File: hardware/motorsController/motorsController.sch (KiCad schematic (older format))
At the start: 1 part

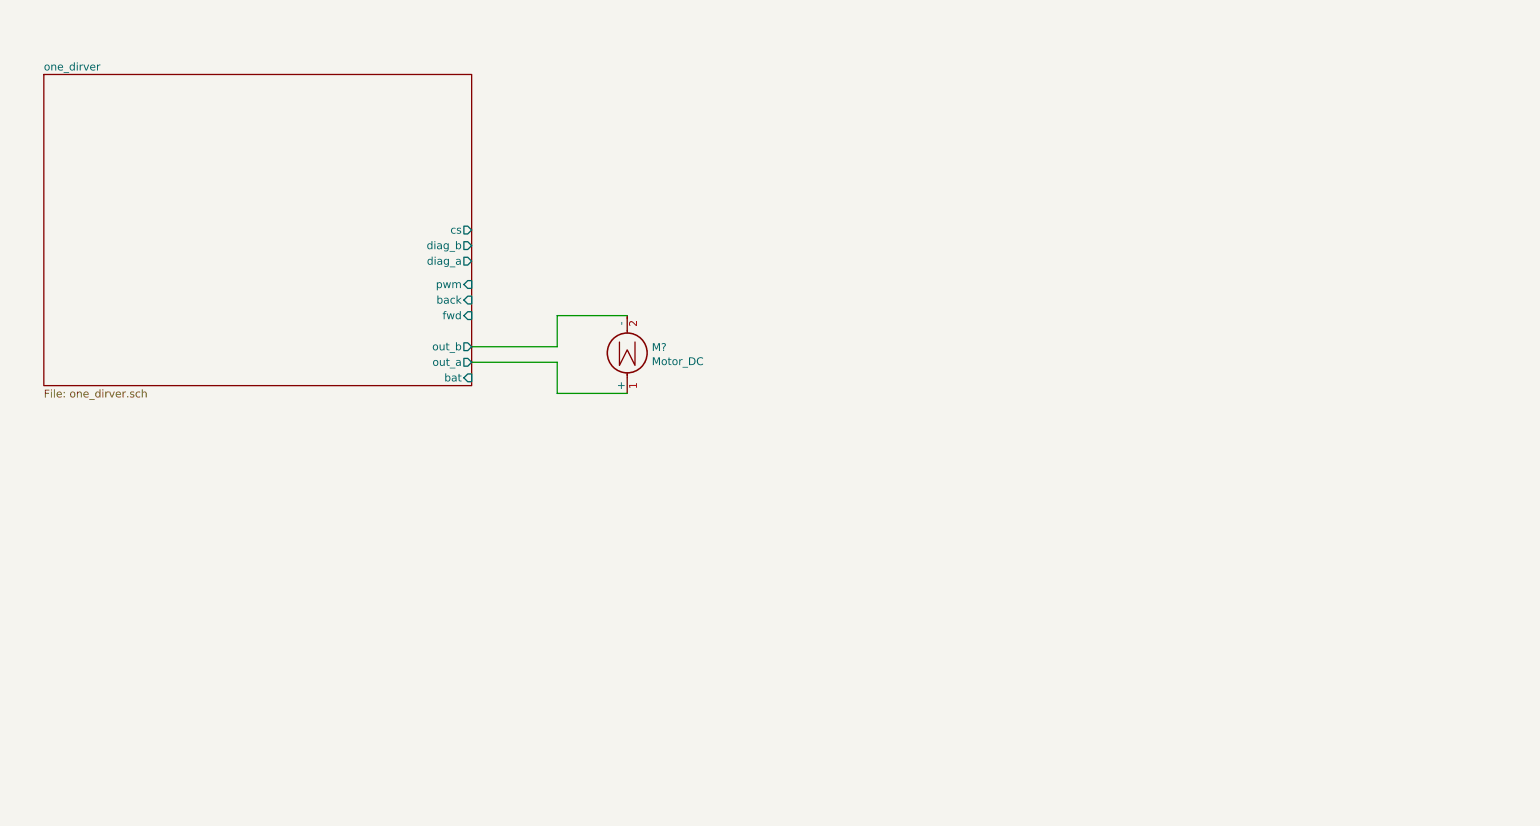
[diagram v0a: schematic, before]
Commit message: layout a pcb for the motor driver IC
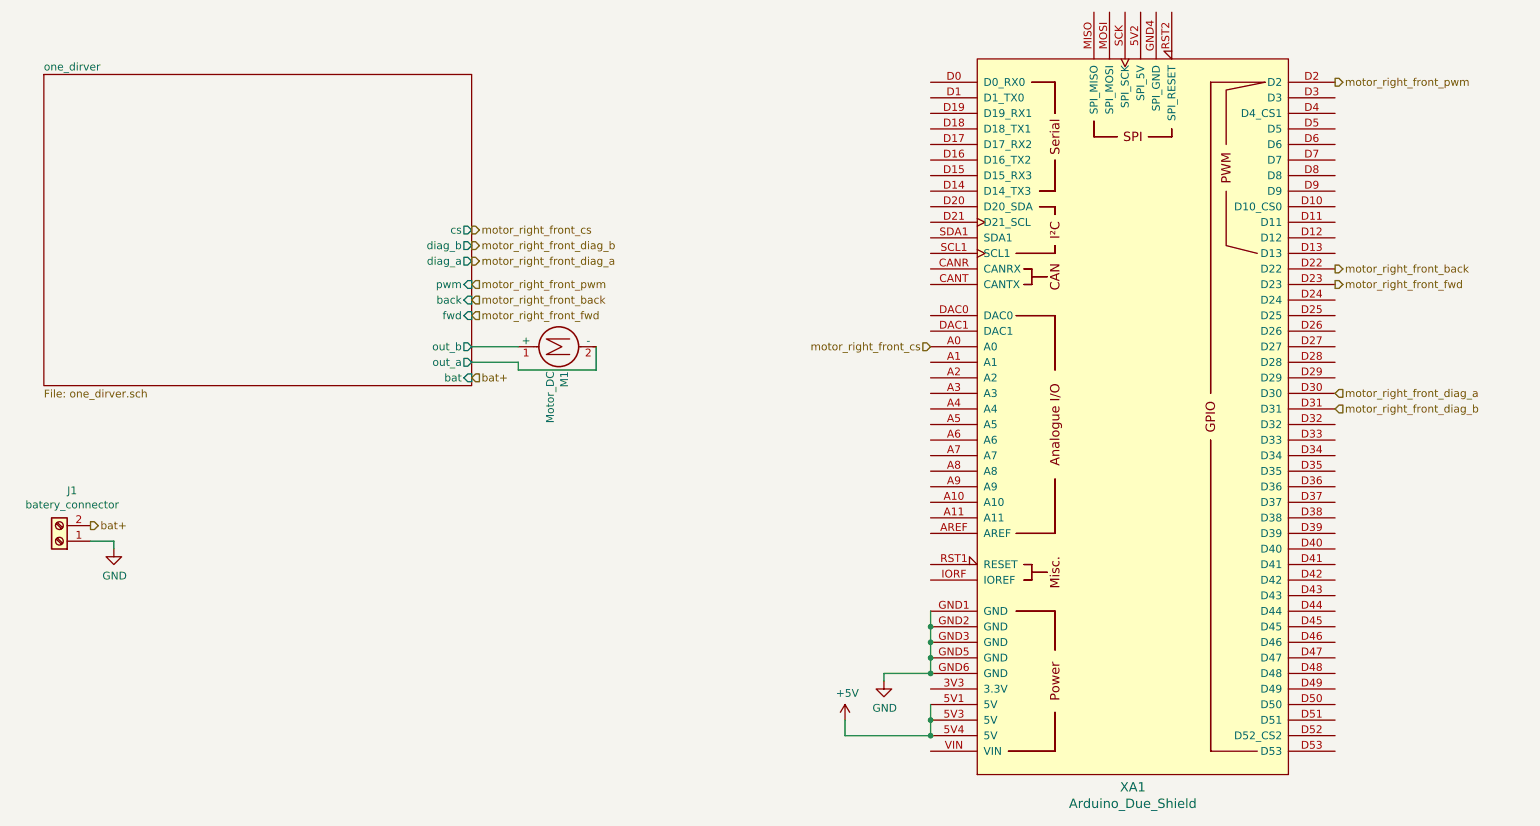
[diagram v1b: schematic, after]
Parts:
- added J1: batery_connector, TerminalBlock:TerminalBlock_bornier-2_P5.08mm, symbol Connector:Screw_Terminal_01x02
- added XA1: Arduino_Due_Shield, Arduino:Arduino_Due_Shield, symbol arduino:Arduino_Due_Shield
- M1: renamed from M?; footprint (none) -> TerminalBlock:TerminalBlock_bornier-2_P5.08mm
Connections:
- net one_dirver/out_a: now also M1.2 (-); no longer M1.1 (+)
- net one_dirver/out_b: now also M1.1 (+); no longer M1.2 (-)
- new net +5V: XA1.5V1 (5V), XA1.5V3 (5V), XA1.5V4 (5V)
- new net GND: J1.1 (Pin_1), XA1.GND1 (GND), XA1.GND2 (GND), XA1.GND3 (GND), XA1.GND5 (GND), XA1.GND6 (GND)
- new net bat+: J1.2 (Pin_2)
- new net motor_right_front_back: XA1.D22
- new net motor_right_front_cs: XA1.A0
- new net motor_right_front_diag_a: XA1.D30
- new net motor_right_front_diag_b: XA1.D31
- new net motor_right_front_fwd: XA1.D23
- new net motor_right_front_pwm: XA1.D2
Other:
- moved on the sheet: M1
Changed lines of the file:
@@
 EELAYER 30 0
 EELAYER END
-$Descr A4 11693 8268
+$Descr A3 16535 11693
 encoding utf-8
 Sheet 1 2
@@
 F10 "bat" I R 4000 3150 50
 $EndSheet
+Text HLabel 4000 2550 2    50   Input ~ 0
+motor_right_front_pwm
 $Comp
-L Motor:Motor_DC M?
+L Motor:Motor_DC M1
 U 1 1 5F794D70
-P 5000 3050
-F 0 "M?" H 4842 2954 50  0000 R CNN
-F 1 "Motor_DC" H 4842 3045 50  0000 R CNN
-F 2 "" H 5000 2960 50  0001 C CNN
-F 3 "~" H 5000 2960 50  0001 C CNN
-	1    5000 3050
+P 4500 2950
+F 0 "M1" H 4342 2854 50  0000 R CNN
+F 1 "Motor_DC" H 4342 2945 50  0000 R CNN
+F 2 "TerminalBlock:TerminalBlock_bornier-2_P5.08mm" H 4500 2860 50  0001 C CNN
+F 3 "~" H 4500 2860 50  0001 C CNN
+	1    4500 2950
+	0    -1   -1   0
+$EndComp
+Wire Wire Line
+	4300 2950 4000 2950
+Wire Wire Line
+	4800 2950 4800 3100
+Wire Wire Line
+	4800 3100 4300 3100
+Wire Wire Line
+	4300 3100 4300 3050
+Wire Wire Line
+	4300 3050 4000 3050
+Text HLabel 4000 2650 2    50   Input ~ 0
+motor_right_front_back
+Text HLabel 4000 2750 2    50   Input ~ 0
+motor_right_front_fwd
+Text HLabel 4000 2200 2    50   Output ~ 0
+motor_right_front_cs
+Text HLabel 4000 2300 2    50   Output ~ 0
+motor_right_front_diag_b
+Text HLabel 4000 2400 2    50   Output ~ 0
+motor_right_front_diag_a
+Text HLabel 9550 1250 2    50   Output ~ 0
+motor_right_front_pwm
+Text HLabel 9550 2450 2    50   Output ~ 0
+motor_right_front_back
+Text HLabel 9550 2550 2    50   Output ~ 0
+motor_right_front_fwd
+Text HLabel 6950 2950 0    50   Input ~ 0
+motor_right_front_cs
+Text HLabel 9550 3350 2    50   Input ~ 0
+motor_right_front_diag_b
+Text HLabel 9550 3250 2    50   Input ~ 0
+motor_right_front_diag_a
+$Comp
+L power:GND #PWR0105
+U 1 1 5F7FA8F7
+P 6650 5100
+F 0 "#PWR0105" H 6650 4850 50  0001 C CNN
+F 1 "GND" H 6655 4927 50  0000 C CNN
+F 2 "" H 6650 5100 50  0001 C CNN
+F 3 "" H 6650 5100 50  0001 C CNN
+	1    6650 5100
+	1    0    0    -1
+$EndComp
+Wire Wire Line
+	6650 5100 6650 5050
+Wire Wire Line
+	6650 5050 6950 5050
+$Comp
+L power:+5V #PWR0106
+U 1 1 5F7FCF51
+P 6400 5350
+F 0 "#PWR0106" H 6400 5200 50  0001 C CNN
+F 1 "+5V" H 6415 5523 50  0000 C CNN
+F 2 "" H 6400 5350 50  0001 C CNN
+F 3 "" H 6400 5350 50  0001 C CNN
+	1    6400 5350
+	1    0    0    -1
+$EndComp
+Wire Wire Line
+	6400 5350 6400 5450
+Wire Wire Line
+	6400 5450 6950 5450
+$Comp
+L Connector:Screw_Terminal_01x02 J1
+U 1 1 5F7F2610
+P 1350 4200
+F 0 "J1" H 1268 3875 50  0000 C CNN
+F 1 "batery_connector" H 1268 3966 50  0000 C CNN
+F 2 "TerminalBlock:TerminalBlock_bornier-2_P5.08mm" H 1350 4200 50  0001 C CNN
+F 3 "~" H 1350 4200 50  0001 C CNN
+	1    1350 4200
 	-1   0    0    1
 $EndComp
+$Comp
+L power:GND #PWR0107
+U 1 1 5F7F3543
+P 1700 4250
+F 0 "#PWR0107" H 1700 4000 50  0001 C CNN
+F 1 "GND" H 1705 4077 50  0000 C CNN
+F 2 "" H 1700 4250 50  0001 C CNN
+F 3 "" H 1700 4250 50  0001 C CNN
+	1    1700 4250
+	1    0    0    -1
+$EndComp
 Wire Wire Line
-	5000 2750 4550 2750
+	1700 4250 1700 4200
 Wire Wire Line
-	4550 2750 4550 2950
+	1700 4200 1550 4200
+Text HLabel 1550 4100 2    50   Output ~ 0
+bat+
+Text HLabel 4000 3150 2    50   Input ~ 0
+bat+
+$Comp
+L arduino:Arduino_Due_Shield XA1
+U 1 1 5F7F0EA5
+P 8250 3400
+F 0 "XA1" H 8250 1019 60  0000 C CNN
+F 1 "Arduino_Due_Shield" H 8250 913 60  0000 C CNN
+F 2 "Arduino:Arduino_Due_Shield" H 8950 6150 60  0001 C CNN
+F 3 "https://store.arduino.cc/arduino-due" H 8950 6150 60  0001 C CNN
+	1    8250 3400
+	1    0    0    -1
+$EndComp
 Wire Wire Line
-	4550 2950 4000 2950
+	6950 5450 6950 5350
+Connection ~ 6950 5450
+Connection ~ 6950 5350
 Wire Wire Line
-	5000 3250 4550 3250
+	6950 5350 6950 5250
 Wire Wire Line
-	4550 3250 4550 3050
+	6950 5050 6950 4950
+Connection ~ 6950 5050
+Connection ~ 6950 4750
 Wire Wire Line
-	4550 3050 4000 3050
+	6950 4750 6950 4650
+Connection ~ 6950 4850
+Wire Wire Line
+	6950 4850 6950 4750
+Connection ~ 6950 4950
+Wire Wire Line
+	6950 4950 6950 4850
 $EndSCHEMATC

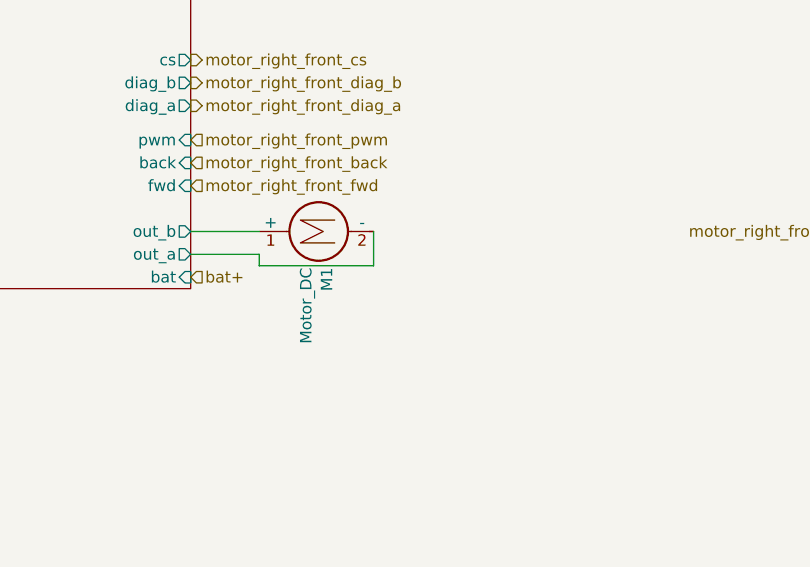
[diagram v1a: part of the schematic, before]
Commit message: reposition motor terminals on both sides of the dirver
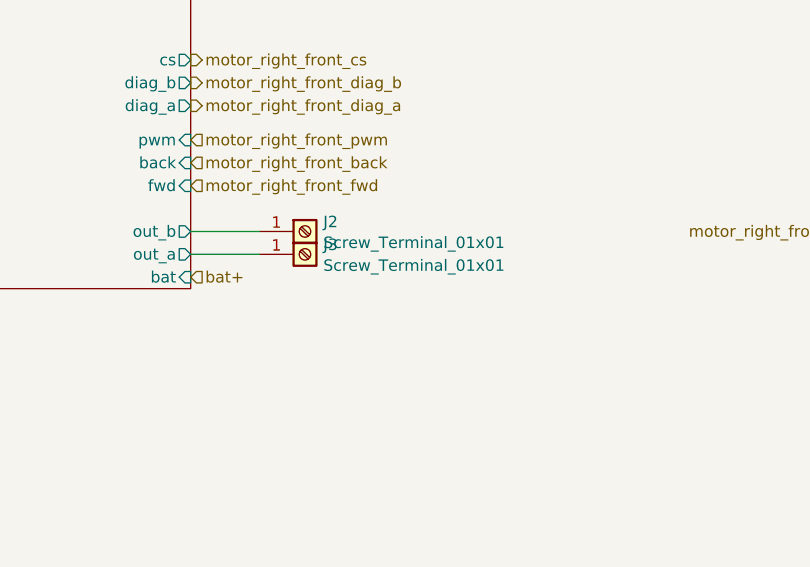
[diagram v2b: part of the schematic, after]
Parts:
- removed M1: Motor_DC, TerminalBlock:TerminalBlock_bornier-2_P5.08mm, symbol Motor:Motor_DC
- added J2, J3: Screw_Terminal_01x01, Connector_Pin:Pin_D1.3mm_L11.3mm_W2.8mm_Flat, symbol Connector:Screw_Terminal_01x01
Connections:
- net one_dirver/out_a: now also J3.1 (Pin_1)
- net one_dirver/out_b: now also J2.1 (Pin_1)
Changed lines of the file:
@@
 Text HLabel 4000 2550 2    50   Input ~ 0
 motor_right_front_pwm
-$Comp
-L Motor:Motor_DC M1
-U 1 1 5F794D70
-P 4500 2950
-F 0 "M1" H 4342 2854 50  0000 R CNN
-F 1 "Motor_DC" H 4342 2945 50  0000 R CNN
-F 2 "TerminalBlock:TerminalBlock_bornier-2_P5.08mm" H 4500 2860 50  0001 C CNN
-F 3 "~" H 4500 2860 50  0001 C CNN
-	1    4500 2950
-	0    -1   -1   0
-$EndComp
 Wire Wire Line
 	4300 2950 4000 2950
-Wire Wire Line
-	4800 2950 4800 3100
-Wire Wire Line
-	4800 3100 4300 3100
-Wire Wire Line
-	4300 3100 4300 3050
 Wire Wire Line
 	4300 3050 4000 3050
@@
 Wire Wire Line
 	6950 4950 6950 4850
+$Comp
+L Connector:Screw_Terminal_01x01 J2
+U 1 1 5F88908C
+P 4500 2950
+F 0 "J2" H 4580 2992 50  0000 L CNN
+F 1 "Screw_Terminal_01x01" H 4580 2901 50  0000 L CNN
+F 2 "Connector_Pin:Pin_D1.3mm_L11.3mm_W2.8mm_Flat" H 4500 2950 50  0001 C CNN
+F 3 "~" H 4500 2950 50  0001 C CNN
+	1    4500 2950
+	1    0    0    -1
+$EndComp
+$Comp
+L Connector:Screw_Terminal_01x01 J3
+U 1 1 5F88A28E
+P 4500 3050
+F 0 "J3" H 4580 3092 50  0000 L CNN
+F 1 "Screw_Terminal_01x01" H 4580 3001 50  0000 L CNN
+F 2 "Connector_Pin:Pin_D1.3mm_L11.3mm_W2.8mm_Flat" H 4500 3050 50  0001 C CNN
+F 3 "~" H 4500 3050 50  0001 C CNN
+	1    4500 3050
+	1    0    0    -1
+$EndComp
 $EndSCHEMATC

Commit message: layout a schema for three more motor drivers
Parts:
- added J? (x6): Screw_Terminal_01x01, Connector_Pin:Pin_D1.3mm_L11.3mm_W2.8mm_Flat, symbol Connector:Screw_Terminal_01x01
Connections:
- net motor_left_front_cs: now reaches XA1.A1
- net motor_right_rear_cs: now reaches XA1.A2
- net motor_left_rear_cs: now reaches XA1.A3
- net motor_left_front_back: now reaches XA1.D24
- net motor_left_front_fwd: now reaches XA1.D25
- net motor_right_rear_back: now reaches XA1.D26
- net motor_right_rear_fwd: now reaches XA1.D27
- net motor_left_rear_back: now reaches XA1.D28
- net motor_left_rear_fwd: now reaches XA1.D29
- net motor_left_front_pwm: now reaches XA1.D3
- net motor_left_front_diag_a: now reaches XA1.D32
- net motor_left_front_diag_b: now reaches XA1.D33
- net motor_right_rear_diag_a: now reaches XA1.D34
- net motor_right_rear_diag_b: now reaches XA1.D35
- net motor_left_rear_diag_a: now reaches XA1.D36
- net motor_left_rear_diag_b: now reaches XA1.D37
- net motor_right_rear_pwm: now reaches XA1.D4 (D4_CS1)
- net motor_left_rear_pwm: now reaches XA1.D5
- new net sheet5F8AE5F8/out_a: J?.1 (Pin_1)
- new net sheet5F8AE5F8/out_b: J?.1 (Pin_1)
- new net sheet5F8B7955/out_a: J?.1 (Pin_1)
- new net sheet5F8B7955/out_b: J?.1 (Pin_1)
- new net sheet5F8B7956/out_a: J?.1 (Pin_1)
- new net sheet5F8B7956/out_b: J?.1 (Pin_1)
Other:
- moved on the sheet: J1, XA1
